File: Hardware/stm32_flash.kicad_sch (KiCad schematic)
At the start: 20 parts, among them IC2 MT29F1G01ABAFDSF-AAT_F_TR, IC3 MT29F1G01ABAFDSF-AAT_F_TR, IC4 MT29F1G01ABAFDSF-AAT_F_TR, IC5 MT29F1G01ABAFDSF-AAT_F_TR

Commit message: prepare for FRAM
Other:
- note added: "Flash"
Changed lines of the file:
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@@
 	(generator_version "9.0")
 	(paper "A3")
+	(text "Flash"
+		(exclude_from_sim no)
+		(at 128.016 74.422 0)
+		(effects
+			(font
+				(size 2.54 2.54)
+			)
+		)
+	)
 	(junction
 		(at 99.06 172.72)

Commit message: Connect connectors
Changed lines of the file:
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@@
 		(on_board yes)
 		(dnp no)
-		(property "Reference" "#PWR056"
+		(property "Reference" "#PWR56"
 			(at 87.63 107.95 0)
 			(effects
@@
 		)
 		(property "Value" "GND"
-			(at 83.82 103.378 0)
+			(at 87.63 105.41 0)
 			(effects
 				(font
@@
 			(project "CTS-SAT-2-OBC-PCB"
 				(path "/58243925-df8d-4fc1-899e-fce866d1d25a/1b38ac1a-71db-4ef7-b830-b2f3080e4569"
-					(reference "#PWR056")
+					(reference "#PWR56")
 					(unit 1)
 				)
@@
 		(dnp no)
 		(fields_autoplaced yes)
-		(property "Reference" "#PWR064"
+		(property "Reference" "#PWR64"
 			(at 160.02 106.68 0)
 			(effects
@@
 			(project "CTS-SAT-2-OBC-PCB"
 				(path "/58243925-df8d-4fc1-899e-fce866d1d25a/1b38ac1a-71db-4ef7-b830-b2f3080e4569"
-					(reference "#PWR064")
+					(reference "#PWR64")
 					(unit 1)
 				)
@@
 		(dnp no)
 		(fields_autoplaced yes)
-		(property "Reference" "#PWR066"
+		(property "Reference" "#PWR66"
 			(at 160.02 144.78 0)
 			(effects
@@
 			(project "CTS-SAT-2-OBC-PCB"
 				(path "/58243925-df8d-4fc1-899e-fce866d1d25a/1b38ac1a-71db-4ef7-b830-b2f3080e4569"
-					(reference "#PWR066")
+					(reference "#PWR66")
 					(unit 1)
 				)
@@
 		(dnp no)
 		(fields_autoplaced yes)
-		(property "Reference" "#PWR070"
+		(property "Reference" "#PWR70"
 			(at 160.02 224.79 0)
 			(effects
@@
 			(project "CTS-SAT-2-OBC-PCB"
 				(path "/58243925-df8d-4fc1-899e-fce866d1d25a/1b38ac1a-71db-4ef7-b830-b2f3080e4569"
-					(reference "#PWR070")
+					(reference "#PWR70")
 					(unit 1)
 				)
@@
 		(on_board yes)
 		(dnp no)
-		(property "Reference" "#PWR057"
+		(property "Reference" "#PWR57"
 			(at 87.63 146.05 0)
 			(effects
@@
 		)
 		(property "Value" "GND"
-			(at 83.82 141.478 0)
+			(at 87.63 143.51 0)
 			(effects
 				(font
@@
 			(project "CTS-SAT-2-OBC-PCB"
 				(path "/58243925-df8d-4fc1-899e-fce866d1d25a/1b38ac1a-71db-4ef7-b830-b2f3080e4569"
-					(reference "#PWR057")
+					(reference "#PWR57")
 					(unit 1)
 				)
@@
 		(on_board yes)
 		(dnp no)
-		(property "Reference" "#PWR058"
+		(property "Reference" "#PWR58"
 			(at 87.63 186.69 0)
 			(effects
@@
 		)
 		(property "Value" "GND"
-			(at 83.82 182.118 0)
+			(at 87.63 184.15 0)
 			(effects
 				(font
@@
 			(project "CTS-SAT-2-OBC-PCB"
 				(path "/58243925-df8d-4fc1-899e-fce866d1d25a/1b38ac1a-71db-4ef7-b830-b2f3080e4569"
-					(reference "#PWR058")
+					(reference "#PWR58")
 					(unit 1)
 				)
@@
 		(dnp no)
 		(fields_autoplaced yes)
-		(property "Reference" "#PWR068"
+		(property "Reference" "#PWR68"
 			(at 160.02 185.42 0)
 			(effects
@@
 			(project "CTS-SAT-2-OBC-PCB"
 				(path "/58243925-df8d-4fc1-899e-fce866d1d25a/1b38ac1a-71db-4ef7-b830-b2f3080e4569"
-					(reference "#PWR068")
+					(reference "#PWR68")
 					(unit 1)
 				)
@@
 		(on_board yes)
 		(dnp no)
-		(property "Reference" "#PWR059"
+		(property "Reference" "#PWR59"
 			(at 87.63 226.06 0)
 			(effects
@@
 		)
 		(property "Value" "GND"
-			(at 83.82 221.488 0)
+			(at 87.63 223.52 0)
 			(effects
 				(font
@@
 			(project "CTS-SAT-2-OBC-PCB"
 				(path "/58243925-df8d-4fc1-899e-fce866d1d25a/1b38ac1a-71db-4ef7-b830-b2f3080e4569"
-					(reference "#PWR059")
-					(unit 1)
-				)
+					(reference "#PWR59")
+					(unit 1)
+				)

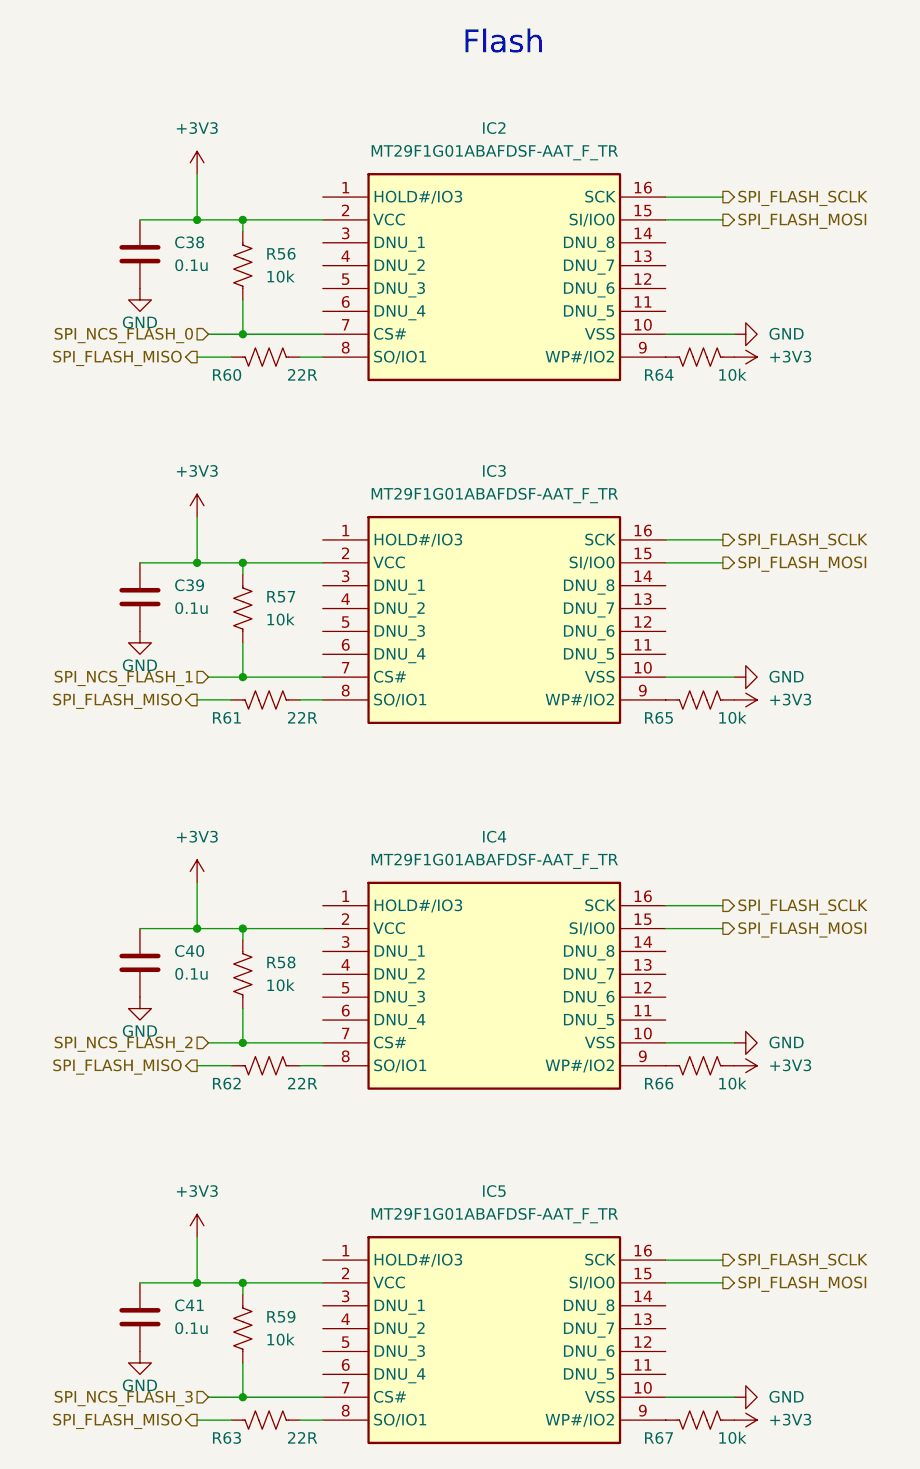
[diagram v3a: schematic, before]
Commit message: Add STM32 Reset Switch & RP2040 I2C pins
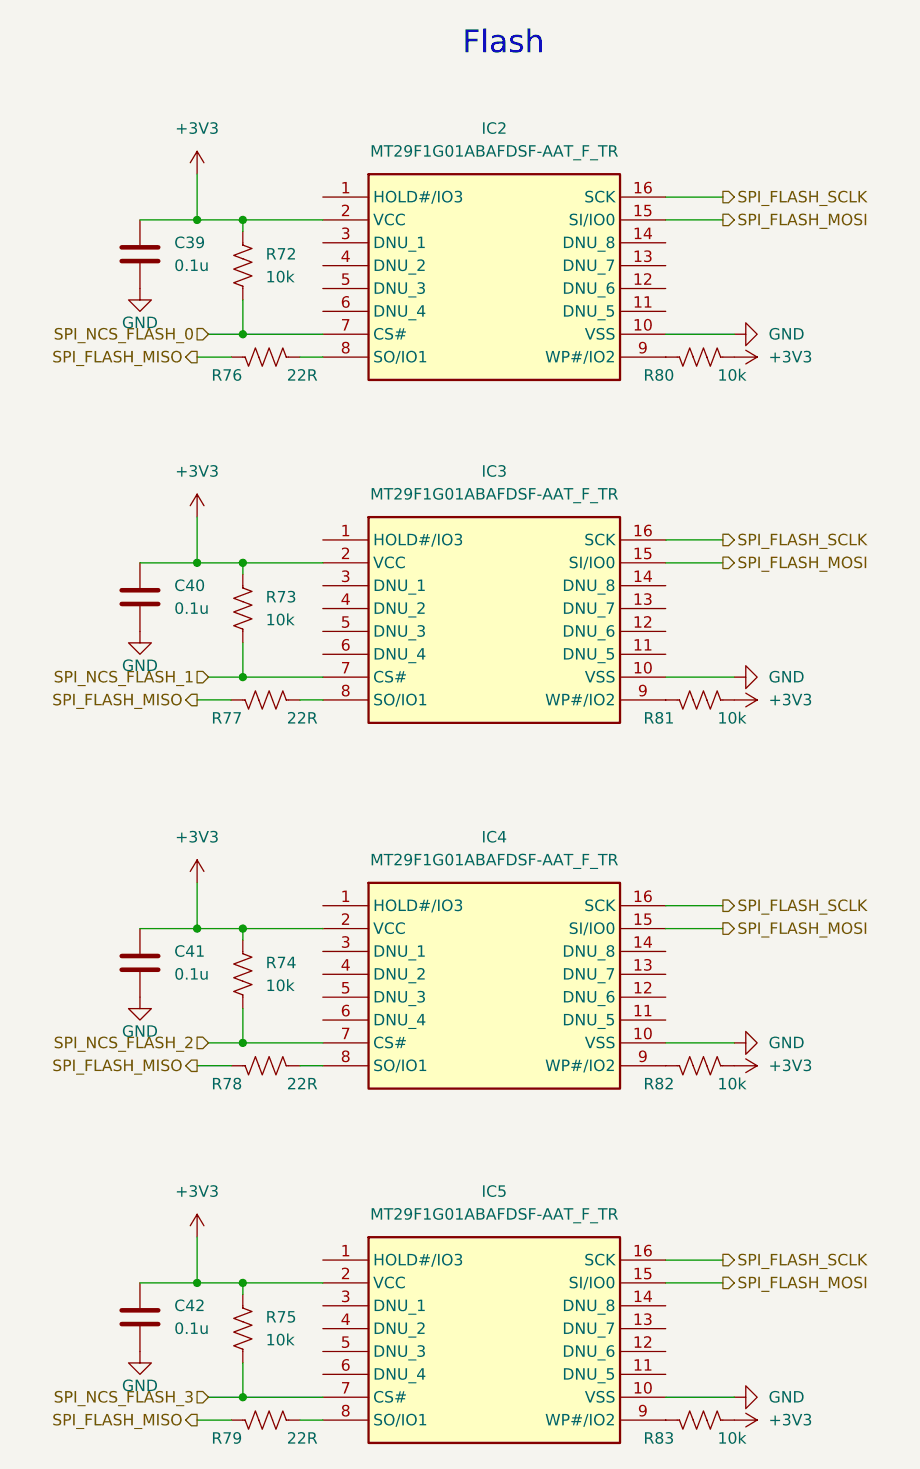
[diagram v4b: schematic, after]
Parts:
- renumbered C38 to C39, C39 to C40, C40 to C41, C41 to C42, R56 to R72, R57 to R73, R58 to R74, R59 to R75, R60 to R76, R61 to R77, R62 to R78, R63 to R79, R64 to R80, R65 to R81, R66 to R82, R67 to R83

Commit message: Add RP2040 SWD
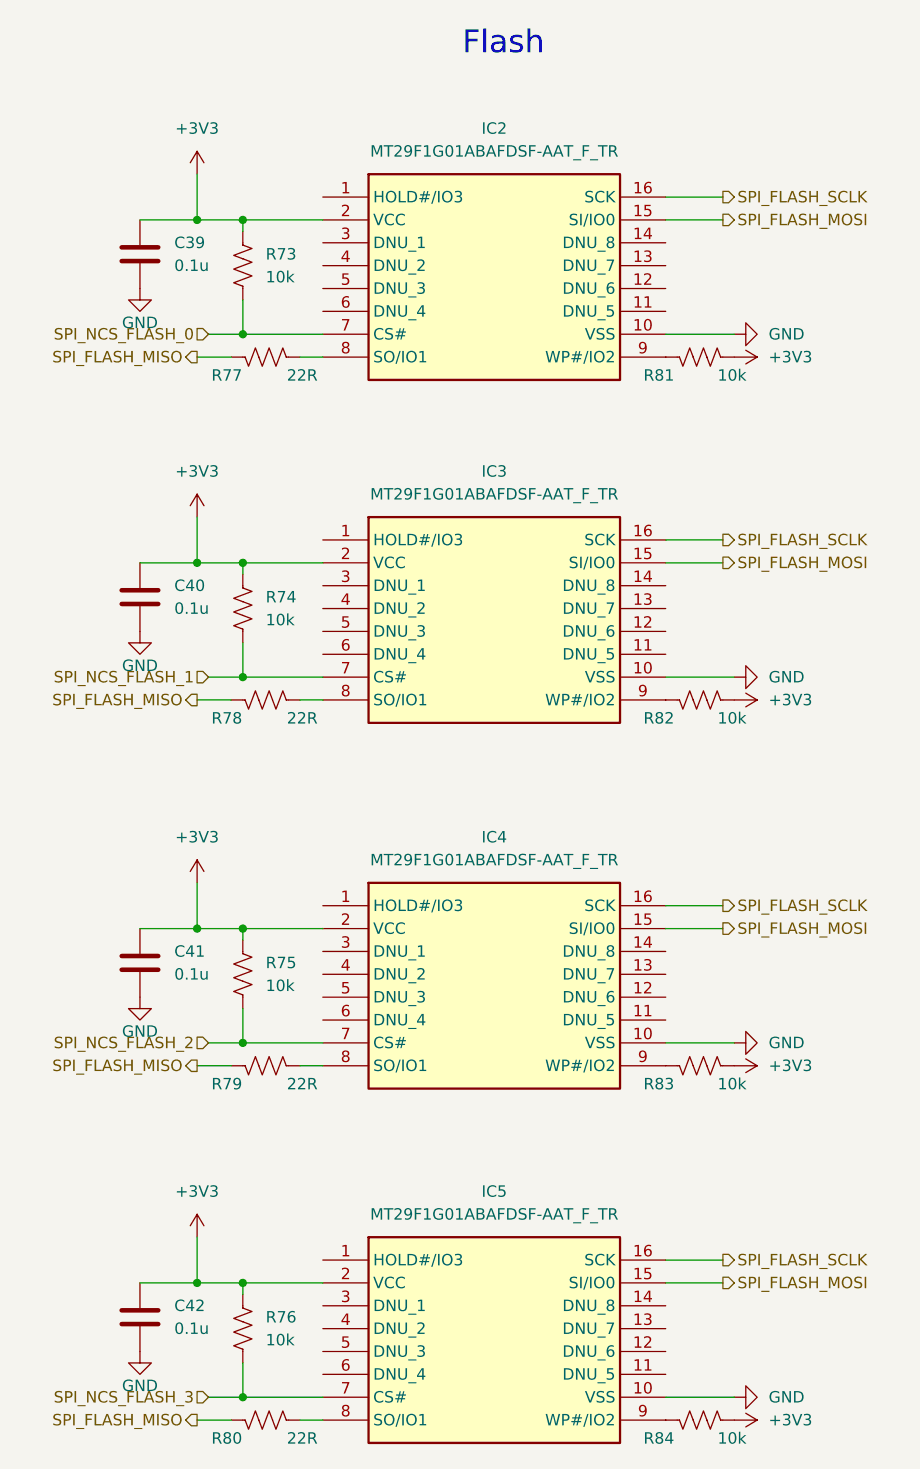
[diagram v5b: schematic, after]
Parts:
- renumbered R72 to R73, R73 to R74, R74 to R75, R75 to R76, R76 to R77, R77 to R78, R78 to R79, R79 to R80, R80 to R81, R81 to R82, R82 to R83, R83 to R84
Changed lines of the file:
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@@
 		(dnp no)
 		(fields_autoplaced yes)
-		(property "Reference" "#PWR097"
+		(property "Reference" "#PWR099"
 			(at 149.86 227.33 0)
 			(effects
@@
 			(project "CTS-SAT-2-OBC-PCB"
 				(path "/58243925-df8d-4fc1-899e-fce866d1d25a/1b38ac1a-71db-4ef7-b830-b2f3080e4569"
-					(reference "#PWR097")
+					(reference "#PWR099")
 					(unit 1)
 				)
@@
 		(on_board yes)
 		(dnp no)
-		(property "Reference" "#PWR082"
+		(property "Reference" "#PWR084"
 			(at 87.63 107.95 0)
 			(effects
@@
 			(project "CTS-SAT-2-OBC-PCB"
 				(path "/58243925-df8d-4fc1-899e-fce866d1d25a/1b38ac1a-71db-4ef7-b830-b2f3080e4569"
-					(reference "#PWR082")
+					(reference "#PWR084")
 					(unit 1)
 				)
@@
 		(on_board yes)
 		(dnp no)
-		(property "Reference" "R78"
+		(property "Reference" "R79"
 			(at 97.282 189.992 90)
 			(effects
@@
 			(project "CTS-SAT-2-OBC-PCB"
 				(path "/58243925-df8d-4fc1-899e-fce866d1d25a/1b38ac1a-71db-4ef7-b830-b2f3080e4569"
-					(reference "R78")
+					(reference "R79")
 					(unit 1)
 				)
@@
 		(dnp no)
 		(fields_autoplaced yes)
-		(property "Reference" "#PWR087"
+		(property "Reference" "#PWR089"
 			(at 93.98 130.81 0)
 			(effects
@@
 			(project "CTS-SAT-2-OBC-PCB"
 				(path "/58243925-df8d-4fc1-899e-fce866d1d25a/1b38ac1a-71db-4ef7-b830-b2f3080e4569"
-					(reference "#PWR087")
+					(reference "#PWR089")
 					(unit 1)
 				)
@@
 		(dnp no)
 		(fields_autoplaced yes)
-		(property "Reference" "R74"
+		(property "Reference" "R75"
 			(at 101.6 176.5299 0)
 			(effects
@@
 			(project "CTS-SAT-2-OBC-PCB"
 				(path "/58243925-df8d-4fc1-899e-fce866d1d25a/1b38ac1a-71db-4ef7-b830-b2f3080e4569"
-					(reference "R74")
+					(reference "R75")
 					(unit 1)
 				)
@@
 		(dnp no)
 		(fields_autoplaced yes)
-		(property "Reference" "R75"
+		(property "Reference" "R76"
 			(at 101.6 215.8999 0)
 			(effects
@@
 			(project "CTS-SAT-2-OBC-PCB"
 				(path "/58243925-df8d-4fc1-899e-fce866d1d25a/1b38ac1a-71db-4ef7-b830-b2f3080e4569"
-					(reference "R75")
+					(reference "R76")
 					(unit 1)
 				)
@@
 		(on_board yes)
 		(dnp no)
-		(property "Reference" "R79"
+		(property "Reference" "R80"
 			(at 97.282 229.362 90)
 			(effects
@@
 			(project "CTS-SAT-2-OBC-PCB"
 				(path "/58243925-df8d-4fc1-899e-fce866d1d25a/1b38ac1a-71db-4ef7-b830-b2f3080e4569"
-					(reference "R79")
+					(reference "R80")
 					(unit 1)
 				)
@@
 		(dnp no)
 		(fields_autoplaced yes)
-		(property "Reference" "#PWR090"
+		(property "Reference" "#PWR092"
 			(at 160.02 106.68 0)
 			(effects
@@
 			(project "CTS-SAT-2-OBC-PCB"
 				(path "/58243925-df8d-4fc1-899e-fce866d1d25a/1b38ac1a-71db-4ef7-b830-b2f3080e4569"
-					(reference "#PWR090")
+					(reference "#PWR092")
 					(unit 1)
 				)
@@
 		(dnp no)
 		(fields_autoplaced yes)
-		(property "Reference" "R72"
+		(property "Reference" "R73"
 			(at 101.6 97.7899 0)
 			(effects
@@
 			(project "CTS-SAT-2-OBC-PCB"
 				(path "/58243925-df8d-4fc1-899e-fce866d1d25a/1b38ac1a-71db-4ef7-b830-b2f3080e4569"
-					(reference "R72")
+					(reference "R73")
 					(unit 1)
 				)
@@
 		(on_board yes)
 		(dnp no)
-		(property "Reference" "R81"
+		(property "Reference" "R82"
 			(at 145.288 149.352 90)
 			(effects
@@
 			(project "CTS-SAT-2-OBC-PCB"
 				(path "/58243925-df8d-4fc1-899e-fce866d1d25a/1b38ac1a-71db-4ef7-b830-b2f3080e4569"
-					(reference "R81")
+					(reference "R82")
 					(unit 1)
 				)
@@
 		(dnp no)
 		(fields_autoplaced yes)
-		(property "Reference" "#PWR092"
+		(property "Reference" "#PWR094"
 			(at 160.02 144.78 0)
 			(effects
@@
 			(project "CTS-SAT-2-OBC-PCB"
 				(path "/58243925-df8d-4fc1-899e-fce866d1d25a/1b38ac1a-71db-4ef7-b830-b2f3080e4569"
-					(reference "#PWR092")
+					(reference "#PWR094")
 					(unit 1)
 				)
@@
 		(dnp no)
 		(fields_autoplaced yes)
-		(property "Reference" "#PWR086"
+		(property "Reference" "#PWR088"
 			(at 93.98 92.71 0)
 			(effects
@@
 			(project "CTS-SAT-2-OBC-PCB"
 				(path "/58243925-df8d-4fc1-899e-fce866d1d25a/1b38ac1a-71db-4ef7-b830-b2f3080e4569"
-					(reference "#PWR086")
+					(reference "#PWR088")
 					(unit 1)
 				)
@@
 		(on_board yes)
 		(dnp no)
-		(property "Reference" "R83"
+		(property "Reference" "R84"
 			(at 145.288 229.362 90)
 			(effects
@@
 			(project "CTS-SAT-2-OBC-PCB"
 				(path "/58243925-df8d-4fc1-899e-fce866d1d25a/1b38ac1a-71db-4ef7-b830-b2f3080e4569"
-					(reference "R83")
+					(reference "R84")
 					(unit 1)
 				)
@@
 		(on_board yes)
 		(dnp no)
-		(property "Reference" "R82"
+		(property "Reference" "R83"
 			(at 145.288 189.992 90)
 			(effects
@@
 			(project "CTS-SAT-2-OBC-PCB"
 				(path "/58243925-df8d-4fc1-899e-fce866d1d25a/1b38ac1a-71db-4ef7-b830-b2f3080e4569"
-					(reference "R82")
+					(reference "R83")
 					(unit 1)
 				)
@@
 		(dnp no)
 		(fields_autoplaced yes)
-		(property "Reference" "#PWR096"
+		(property "Reference" "#PWR098"
 			(at 160.02 224.79 0)
 			(effects
@@
 			(project "CTS-SAT-2-OBC-PCB"
 				(path "/58243925-df8d-4fc1-899e-fce866d1d25a/1b38ac1a-71db-4ef7-b830-b2f3080e4569"
-					(reference "#PWR096")
+					(reference "#PWR098")
 					(unit 1)
 				)
@@
 		(on_board yes)
 		(dnp no)
-		(property "Reference" "#PWR083"
+		(property "Reference" "#PWR085"
 			(at 87.63 146.05 0)
 			(effects
@@
 			(project "CTS-SAT-2-OBC-PCB"
 				(path "/58243925-df8d-4fc1-899e-fce866d1d25a/1b38ac1a-71db-4ef7-b830-b2f3080e4569"
-					(reference "#PWR083")
+					(reference "#PWR085")
 					(unit 1)
 				)
@@
 		(dnp no)
 		(fields_autoplaced yes)
-		(property "Reference" "#PWR093"
+		(property "Reference" "#PWR095"
 			(at 149.86 147.32 0)
 			(effects
@@
 			(project "CTS-SAT-2-OBC-PCB"
 				(path "/58243925-df8d-4fc1-899e-fce866d1d25a/1b38ac1a-71db-4ef7-b830-b2f3080e4569"
-					(reference "#PWR093")
+					(reference "#PWR095")
 					(unit 1)
 				)
@@
 		(dnp no)
 		(fields_autoplaced yes)
-		(property "Reference" "R73"
+		(property "Reference" "R74"
 			(at 101.6 135.8899 0)
 			(effects
@@
 			(project "CTS-SAT-2-OBC-PCB"
 				(path "/58243925-df8d-4fc1-899e-fce866d1d25a/1b38ac1a-71db-4ef7-b830-b2f3080e4569"
-					(reference "R73")
+					(reference "R74")
 					(unit 1)
 				)
@@
 		(on_board yes)
 		(dnp no)
-		(property "Reference" "#PWR084"
+		(property "Reference" "#PWR086"
 			(at 87.63 186.69 0)
 			(effects
@@
 			(project "CTS-SAT-2-OBC-PCB"
 				(path "/58243925-df8d-4fc1-899e-fce866d1d25a/1b38ac1a-71db-4ef7-b830-b2f3080e4569"
-					(reference "#PWR084")
+					(reference "#PWR086")
 					(unit 1)
 				)
@@
 		(dnp no)
 		(fields_autoplaced yes)
-		(property "Reference" "#PWR094"
+		(property "Reference" "#PWR096"
 			(at 160.02 185.42 0)
 			(effects
@@
 			(project "CTS-SAT-2-OBC-PCB"
 				(path "/58243925-df8d-4fc1-899e-fce866d1d25a/1b38ac1a-71db-4ef7-b830-b2f3080e4569"
-					(reference "#PWR094")
+					(reference "#PWR096")
 					(unit 1)
 				)
@@
 		(on_board yes)
 		(dnp no)
-		(property "Reference" "#PWR085"
+		(property "Reference" "#PWR087"
 			(at 87.63 226.06 0)
 			(effects
@@
 			(project "CTS-SAT-2-OBC-PCB"
 				(path "/58243925-df8d-4fc1-899e-fce866d1d25a/1b38ac1a-71db-4ef7-b830-b2f3080e4569"
-					(reference "#PWR085")
+					(reference "#PWR087")
 					(unit 1)
 				)
@@
 		(dnp no)
 		(fields_autoplaced yes)
-		(property "Reference" "#PWR095"
+		(property "Reference" "#PWR097"
 			(at 149.86 187.96 0)
 			(effects
@@
 			(project "CTS-SAT-2-OBC-PCB"
 				(path "/58243925-df8d-4fc1-899e-fce866d1d25a/1b38ac1a-71db-4ef7-b830-b2f3080e4569"
-					(reference "#PWR095")
+					(reference "#PWR097")
 					(unit 1)
 				)
@@
 		(dnp no)
 		(fields_autoplaced yes)
-		(property "Reference" "#PWR091"
+		(property "Reference" "#PWR093"
 			(at 149.86 109.22 0)
 			(effects
@@
 			(project "CTS-SAT-2-OBC-PCB"
 				(path "/58243925-df8d-4fc1-899e-fce866d1d25a/1b38ac1a-71db-4ef7-b830-b2f3080e4569"
-					(reference "#PWR091")
+					(reference "#PWR093")
 					(unit 1)
 				)
@@
 		(dnp no)
 		(fields_autoplaced yes)
-		(property "Reference" "#PWR089"
+		(property "Reference" "#PWR091"
 			(at 93.98 210.82 0)
 			(effects
@@
 			(project "CTS-SAT-2-OBC-PCB"
 				(path "/58243925-df8d-4fc1-899e-fce866d1d25a/1b38ac1a-71db-4ef7-b830-b2f3080e4569"
-					(reference "#PWR089")
+					(reference "#PWR091")
 					(unit 1)
 				)
@@
 		(on_board yes)
 		(dnp no)
-		(property "Reference" "R80"
+		(property "Reference" "R81"
 			(at 145.288 111.252 90)
 			(effects
@@
 			(project "CTS-SAT-2-OBC-PCB"
 				(path "/58243925-df8d-4fc1-899e-fce866d1d25a/1b38ac1a-71db-4ef7-b830-b2f3080e4569"
-					(reference "R80")
+					(reference "R81")
 					(unit 1)
 				)
@@
 		(dnp no)
 		(fields_autoplaced yes)
-		(property "Reference" "#PWR088"
+		(property "Reference" "#PWR090"
 			(at 93.98 171.45 0)
 			(effects
@@
 			(project "CTS-SAT-2-OBC-PCB"
 				(path "/58243925-df8d-4fc1-899e-fce866d1d25a/1b38ac1a-71db-4ef7-b830-b2f3080e4569"
-					(reference "#PWR088")
+					(reference "#PWR090")
 					(unit 1)
 				)
@@
 		(on_board yes)
 		(dnp no)
-		(property "Reference" "R76"
+		(property "Reference" "R77"
 			(at 97.282 111.252 90)
 			(effects
@@
 			(project "CTS-SAT-2-OBC-PCB"
 				(path "/58243925-df8d-4fc1-899e-fce866d1d25a/1b38ac1a-71db-4ef7-b830-b2f3080e4569"
-					(reference "R76")
+					(reference "R77")
 					(unit 1)
 				)
@@
 		(on_board yes)
 		(dnp no)
-		(property "Reference" "R77"
+		(property "Reference" "R78"
 			(at 97.282 149.352 90)
 			(effects
@@
 			(project "CTS-SAT-2-OBC-PCB"
 				(path "/58243925-df8d-4fc1-899e-fce866d1d25a/1b38ac1a-71db-4ef7-b830-b2f3080e4569"
-					(reference "R77")
-					(unit 1)
-				)
+					(reference "R78")
+					(unit 1)
+				)
